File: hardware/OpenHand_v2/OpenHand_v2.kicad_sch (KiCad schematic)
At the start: 56 parts, among them J1 CONN_MOTOR_1, J10 CONN_FDBK_2, J11 CONN_EMG_2, J12 CONN_POS_3, J13 CONN_JTAG, J2 CONN_MOTOR_2, J3 CONN_BATT, J4 CONN_POS_1, J5 USB_C_CONN, J6 CONN_MOTOR_3, J7 CONN_FDBK_1, J8 CONN_EMG_1, J9 CONN_POS_2, SW1 BTN_RST, SW3 SW_Push, U1 STM32F103RETx, Y1 16MHz

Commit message: Update V2 schematic and start PCB layout
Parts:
- removed J5: USB_C_CONN, Connector_USB:USB_C_Receptacle_G-Switch_GT-USB-7010ASV, symbol Connector:USB_C_Receptacle_USB2.0
- removed JP2: JMPR_LED_1, Jumper:SolderJumper-2_P1.3mm_Bridged_RoundedPad1.0x1.5mm, symbol Jumper:SolderJumper_2_Bridged
- removed JP3: JMPR_BTN_1, Jumper:SolderJumper-2_P1.3mm_Bridged_RoundedPad1.0x1.5mm, symbol Jumper:SolderJumper_2_Bridged
- removed JP4: JMPR_LED_2, Jumper:SolderJumper-2_P1.3mm_Bridged_RoundedPad1.0x1.5mm, symbol Jumper:SolderJumper_2_Bridged
- removed R4: 1.5k, Resistor_SMD:R_0805_2012Metric, symbol Device:R
- removed TP12: TP_UC_PIN_PA5, TestPoint:TestPoint_Pad_D1.0mm, symbol Connector:TestPoint_Small
- removed TP13: TP_UC_PIN_PD2, TestPoint:TestPoint_Pad_D1.0mm, symbol Connector:TestPoint_Small
- removed TP14: TP_UC_PIN_PA6, TestPoint:TestPoint_Pad_D1.0mm, symbol Connector:TestPoint_Small
- removed TP20: TP_UC_PIN_PC12, TestPoint:TestPoint_Pad_D1.0mm, symbol Connector:TestPoint_Small
- removed TP23: TP_UC_PIN_PB12, TestPoint:TestPoint_Pad_D1.0mm, symbol Connector:TestPoint_Small
- added J5: CONN_USB_C, Connector_USB:USB_C_Receptacle_G-Switch_GT-USB-7010ASV, symbol Connector:USB_C_Receptacle_USB2.0_16P
- added R3: 1.5k, Resistor_SMD:R_0805_2012Metric, symbol Device:R
- J10: renamed from J13; footprint (none) -> Connector_PinHeader_2.54mm:PinHeader_1x06_P2.54mm_Vertical
- J12: renamed from J11; footprint Connector_JST:JST_EH_S3B-EH_1x03_P2.50mm_Horizontal -> Connector_PinHeader_2.54mm:PinHeader_1x03_P2.54mm_Vertical
- J13: renamed from J12; footprint Connector_JST:JST_EH_S3B-EH_1x03_P2.50mm_Horizontal -> Connector_PinHeader_2.54mm:PinHeader_1x03_P2.54mm_Vertical
- J4, J8, J9: footprint Connector_JST:JST_EH_S3B-EH_1x03_P2.50mm_Horizontal -> Connector_PinHeader_2.54mm:PinHeader_1x03_P2.54mm_Vertical
- Y1: footprint (none) -> Crystal:Crystal_SMD_3225-4Pin_3.2x2.5mm; Footprint Desc (none) -> SMD3225-4P
- renumbered C3 to C2, C4 to C3, C5 to C4, C6 to C5, C40 to C6, C2 to C7, C15 to C8, J10 to J11, R2 to R1, R11 to R10, R12 to R11, R3 to R2, R6 to R4, R7 to R5, R8 to R6, R9 to R7, R10 to R8, R5 to R9, SW3 to SW2, TP18 to TP1, TP19 to TP2, TP21 to TP3, TP22 to TP4
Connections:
- net Earth is gone; now on net GND: C1.2, C2.2, C3.2, C4.2, C5.2, C6.2, H1.1, H2.1, H3.1, H4.1, J10.1 (Pin_1), J12.1 (Pin_1), J13.1 (Pin_1), J3.1 (Pin_1), J4.1 (Pin_1), J8.1 (Pin_1), J9.1 (Pin_1), R1.2, R11.1, R2.2, R7.2, R8.2, R9.1, RV1.1, RV2.1, SW1.2, SW2.2, U1.12 (VSSA), U1.18 (VSS), U1.31 (VSS), U1.47 (VSS), U1.63 (VSS)
- net HW_REV_04 is gone; now on net HSE_IN: U1.5 (PD0)
- net +3V3: now also R3.2
- net +5V: now also J5.A4 (VBUS), J5.A9 (VBUS), J5.B4 (VBUS), J5.B9 (VBUS)
- net BTN_01: now also R6.2, SW2.1
- net LED_1: now also D1.2 (A)
- net LED_2: now also D2.2 (A)
- net USB_D+: now also J5.A6 (D+), J5.B6 (D+), R3.1
- net USB_D-: now also J5.A7 (D-), J5.B7 (D-)
- net HSE_IN: now reaches Y1.1
- net HSE_IN: now also C7.1
- net GND: now reaches Y1.2
- net GND: now also C7.2, C8.2, Y1.4, J5.A1 (GND), J5.A12 (GND), J5.B1 (GND), J5.B12 (GND)
- net HSE_OUT: now reaches Y1.3
- net HSE_OUT: now also C8.1, U1.6 (PD1)
- net LED_1_K: now reaches D1.1 (K), R7.1
- net USB_CC2: now reaches R2.1
- net USB_CC2: now also J5.B5 (CC2)
- net USB_CC1: now reaches R1.1
- net USB_CC1: now also J5.A5 (CC1)
- net UC_BOOT: now reaches R9.2, U1.60 (BOOT0)
- net LED_2_K: now reaches D2.1 (K), R8.1
- net HW_REV_01: no longer names the net of U1.2 (PC13)
- net HW_REV_02: no longer names the net of U1.3 (PC14)
- net HW_REV_03: no longer names the net of U1.4 (PC15)
- net TRIM_POT_03: no longer names the net of U1.14 (PA0)
- no-connect marks 4 -> 12
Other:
- note added: "HSE - External oscillator CL = 2*(CL0-Cs) = 2*(10-5)pF = 10pF"
- note added: "TODO: - Add JLC order number on PCB - Double-check all the footprint sizes and dimensions - Order additional parts (osc, caps, buttons...)"
- note removed: "TODO: - Add JLC order number on PCB - Double-check all the footprint sizes and dimensions"
- note removed: "TODO: clock oscillator"
- moved on the sheet: C7, C8, D1, D2, R1, R10, R11, R2, R6, R7, R8, R9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

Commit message: Add V2 PCB and update CubeIDE config for V2
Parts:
- removed J10: CONN_JTAG, Connector_PinHeader_2.54mm:PinHeader_1x06_P2.54mm_Vertical, symbol Connector_Generic:Conn_01x06
- added C6: 100n, Capacitor_SMD:C_0805_2012Metric, symbol Device:C
- added J12: CONN_SWD, Connector_PinHeader_2.54mm:PinHeader_1x04_P2.54mm_Vertical, symbol Connector_Generic:Conn_01x04
- added TP1: TP_UC_PA6, TestPoint:TestPoint_Pad_D1.0mm, symbol Connector:TestPoint_Small
- added TP10: TP_GND_5, TestPoint:TestPoint_Pad_1.5x1.5mm, symbol Connector:TestPoint_Small
- added TP11: TP_GND_6, TestPoint:TestPoint_Pad_1.5x1.5mm, symbol Connector:TestPoint_Small
- added TP14: TP_UC_PB12, TestPoint:TestPoint_Pad_D1.0mm, symbol Connector:TestPoint_Small
- added TP4: TP_UC_PC13, TestPoint:TestPoint_Pad_D1.0mm, symbol Connector:TestPoint_Small
- added TP5: TP_UC_PC15, TestPoint:TestPoint_Pad_D1.0mm, symbol Connector:TestPoint_Small
- added TP6: TP_GND_1, TestPoint:TestPoint_Pad_1.5x1.5mm, symbol Connector:TestPoint_Small
- added TP7: TP_GND_2, TestPoint:TestPoint_Pad_1.5x1.5mm, symbol Connector:TestPoint_Small
- added TP8: TP_GND_3, TestPoint:TestPoint_Pad_1.5x1.5mm, symbol Connector:TestPoint_Small
- added TP9: TP_GND_4, TestPoint:TestPoint_Pad_1.5x1.5mm, symbol Connector:TestPoint_Small
- TP12: renamed from TP3; footprint TestPoint:TestPoint_Pad_D1.0mm -> TestPoint:TestPoint_Pad_D2.0mm
- TP13: renamed from TP4; footprint TestPoint:TestPoint_Pad_D1.0mm -> TestPoint:TestPoint_Pad_D2.0mm
- TP2: renamed from TP1; footprint TestPoint:TestPoint_Pad_D1.0mm -> TestPoint:TestPoint_Pad_D2.0mm
- TP3: renamed from TP2; footprint TestPoint:TestPoint_Pad_D1.0mm -> TestPoint:TestPoint_Pad_D2.0mm
- renumbered C6 to C7, C7 to C8, C8 to C9, J11 to J10, J12 to J11
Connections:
- net +3V3: now also C6.1, J12.4 (Pin_4)
- net GND: now also C6.2, J12.1 (Pin_1), TP10.1, TP11.1, TP6.1, TP7.1, TP8.1, TP9.1
- net HAPTIC_01_DIR: now also U1.34 (PB13); no longer U1.36 (PB15)
- net HAPTIC_01_PWM: now also U1.35 (PB14); no longer U1.37 (PC6)
- net HAPTIC_02_DIR: now also U1.36 (PB15); no longer U1.34 (PB13)
- net HAPTIC_02_PWM: now also U1.37 (PC6); no longer U1.35 (PB14)
- net HAPTIC_EN: now also U1.23 (PA7); no longer U1.26 (PB0)
- net MOTOR_01_DIR: now also U1.38 (PC7); no longer U1.42 (PA9)
- net MOTOR_01_EN: now also U1.25 (PC5); no longer U1.23 (PA7)
- net MOTOR_01_FAULT: now also U1.28 (PB2); no longer U1.27 (PB1)
- net MOTOR_01_PWM: now also U1.39 (PC8); no longer U1.43 (PA10)
- net MOTOR_02_EN: now also U1.27 (PB1); no longer U1.24 (PC4)
- net MOTOR_02_FAULT: now also U1.26 (PB0); no longer U1.28 (PB2)
- net MOTOR_03_DIR: now also U1.42 (PA9); no longer U1.38 (PC7)
- net MOTOR_03_EN: now also U1.29 (PB10); no longer U1.25 (PC5)
- net MOTOR_03_FAULT: now also U1.24 (PC4); no longer U1.29 (PB10)
- net MOTOR_03_PWM: now also U1.43 (PA10); no longer U1.39 (PC8)
- net at U1.2 (PC13): now also TP4.1
- net at U1.22 (PA6): now also TP1.1
- net at U1.33 (PB12): now also TP14.1
- net at U1.4 (PC15): now also TP5.1
- net JTAG_RST: no longer names the net of U1.56 (PB4)
- net JTAG_TCK renamed SWCLK
- net SWCLK: now also J12.3 (Pin_3)
- net JTAG_TDI: no longer names the net of U1.50 (PA15)
- net JTAG_TDO: no longer names the net of U1.55 (PB3)
- net JTAG_TMS renamed SWDIO
- net SWDIO: now also J12.2 (Pin_2)
- no-connect marks 12 -> 11
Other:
- note added: "Can be useful sometimes. To be placed around the board"
- note added: "GROUND TEST POINTS"
- note added: "Serial Wire Debug"
- note added: "Serial Wire Debug (SWD)"
- note removed: "JTAG"
- note removed: "JTAG debugging"
- moved on the sheet: C7

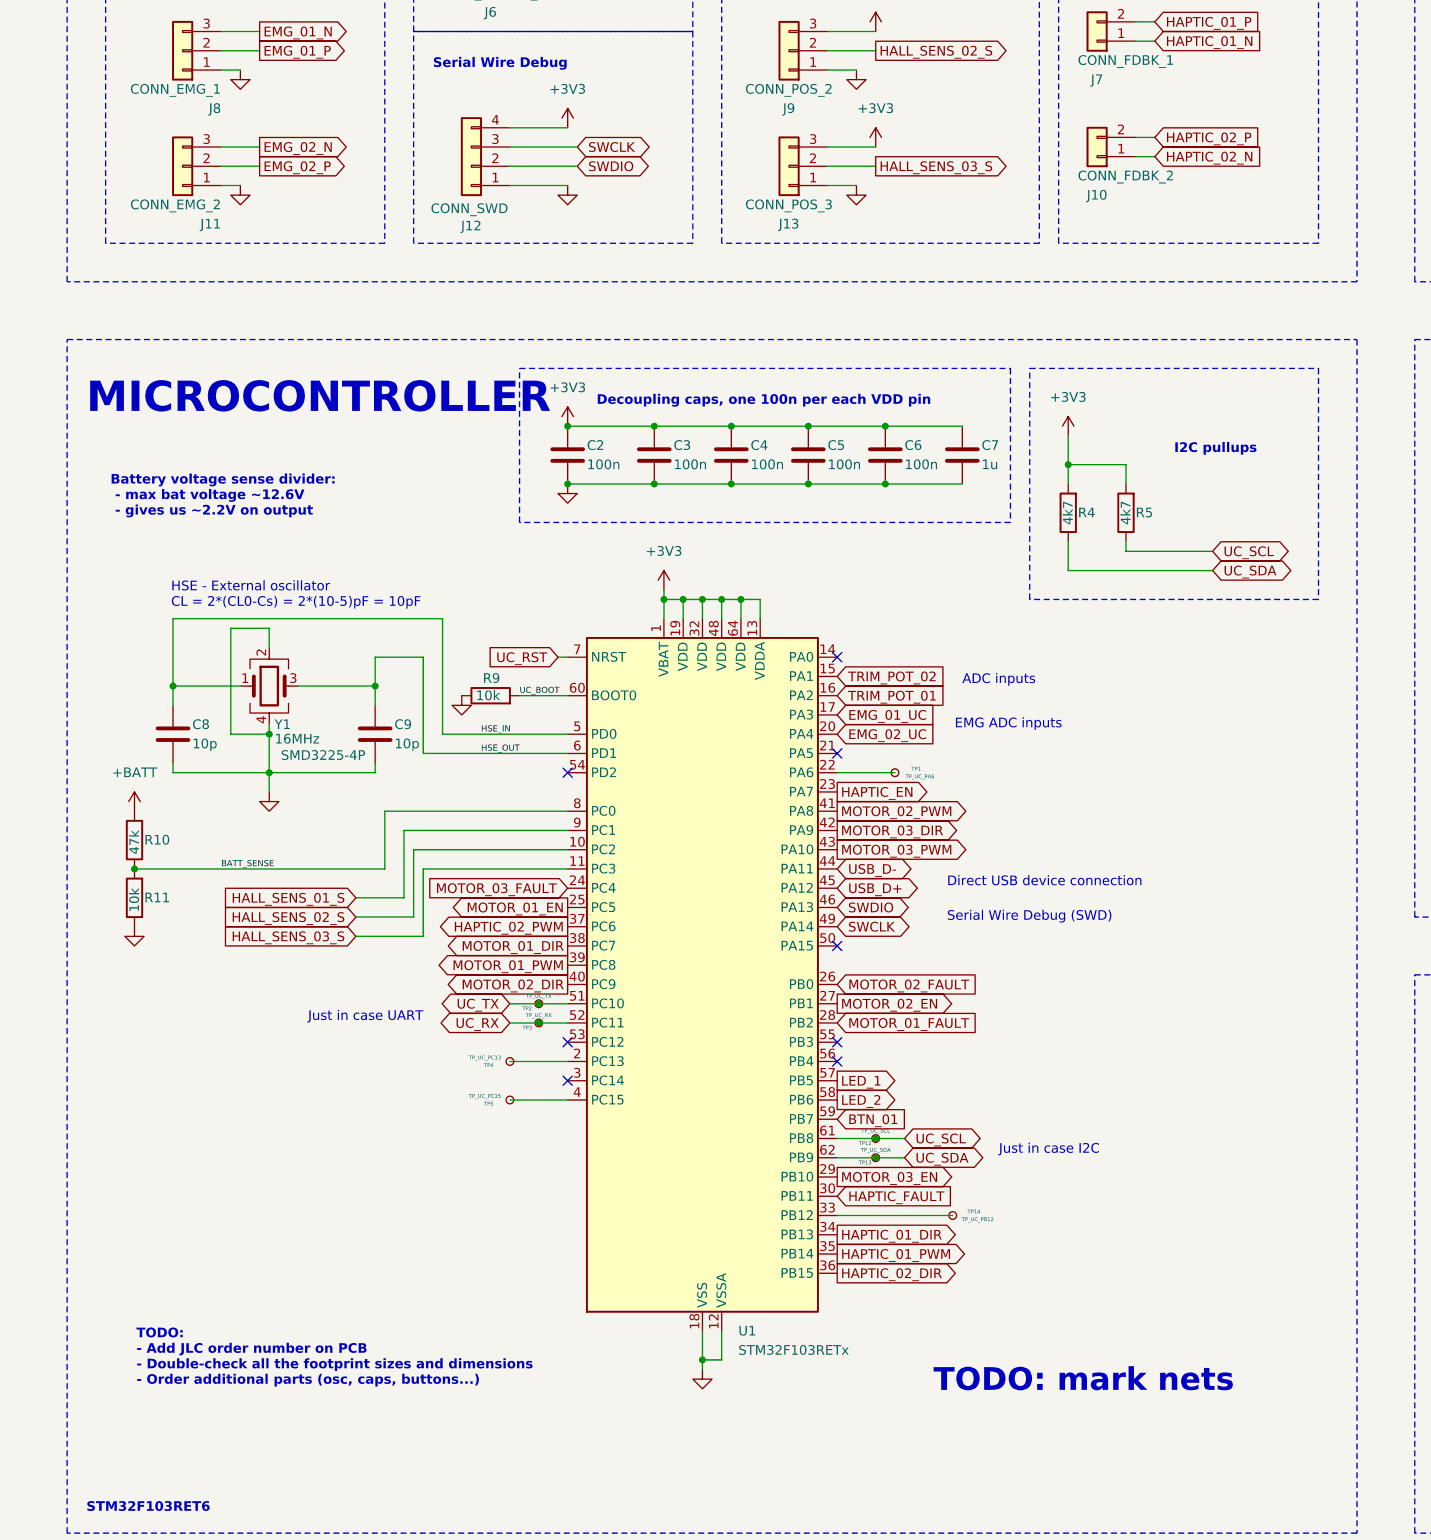
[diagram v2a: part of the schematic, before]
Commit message: Update PCB and order from JLCPCB
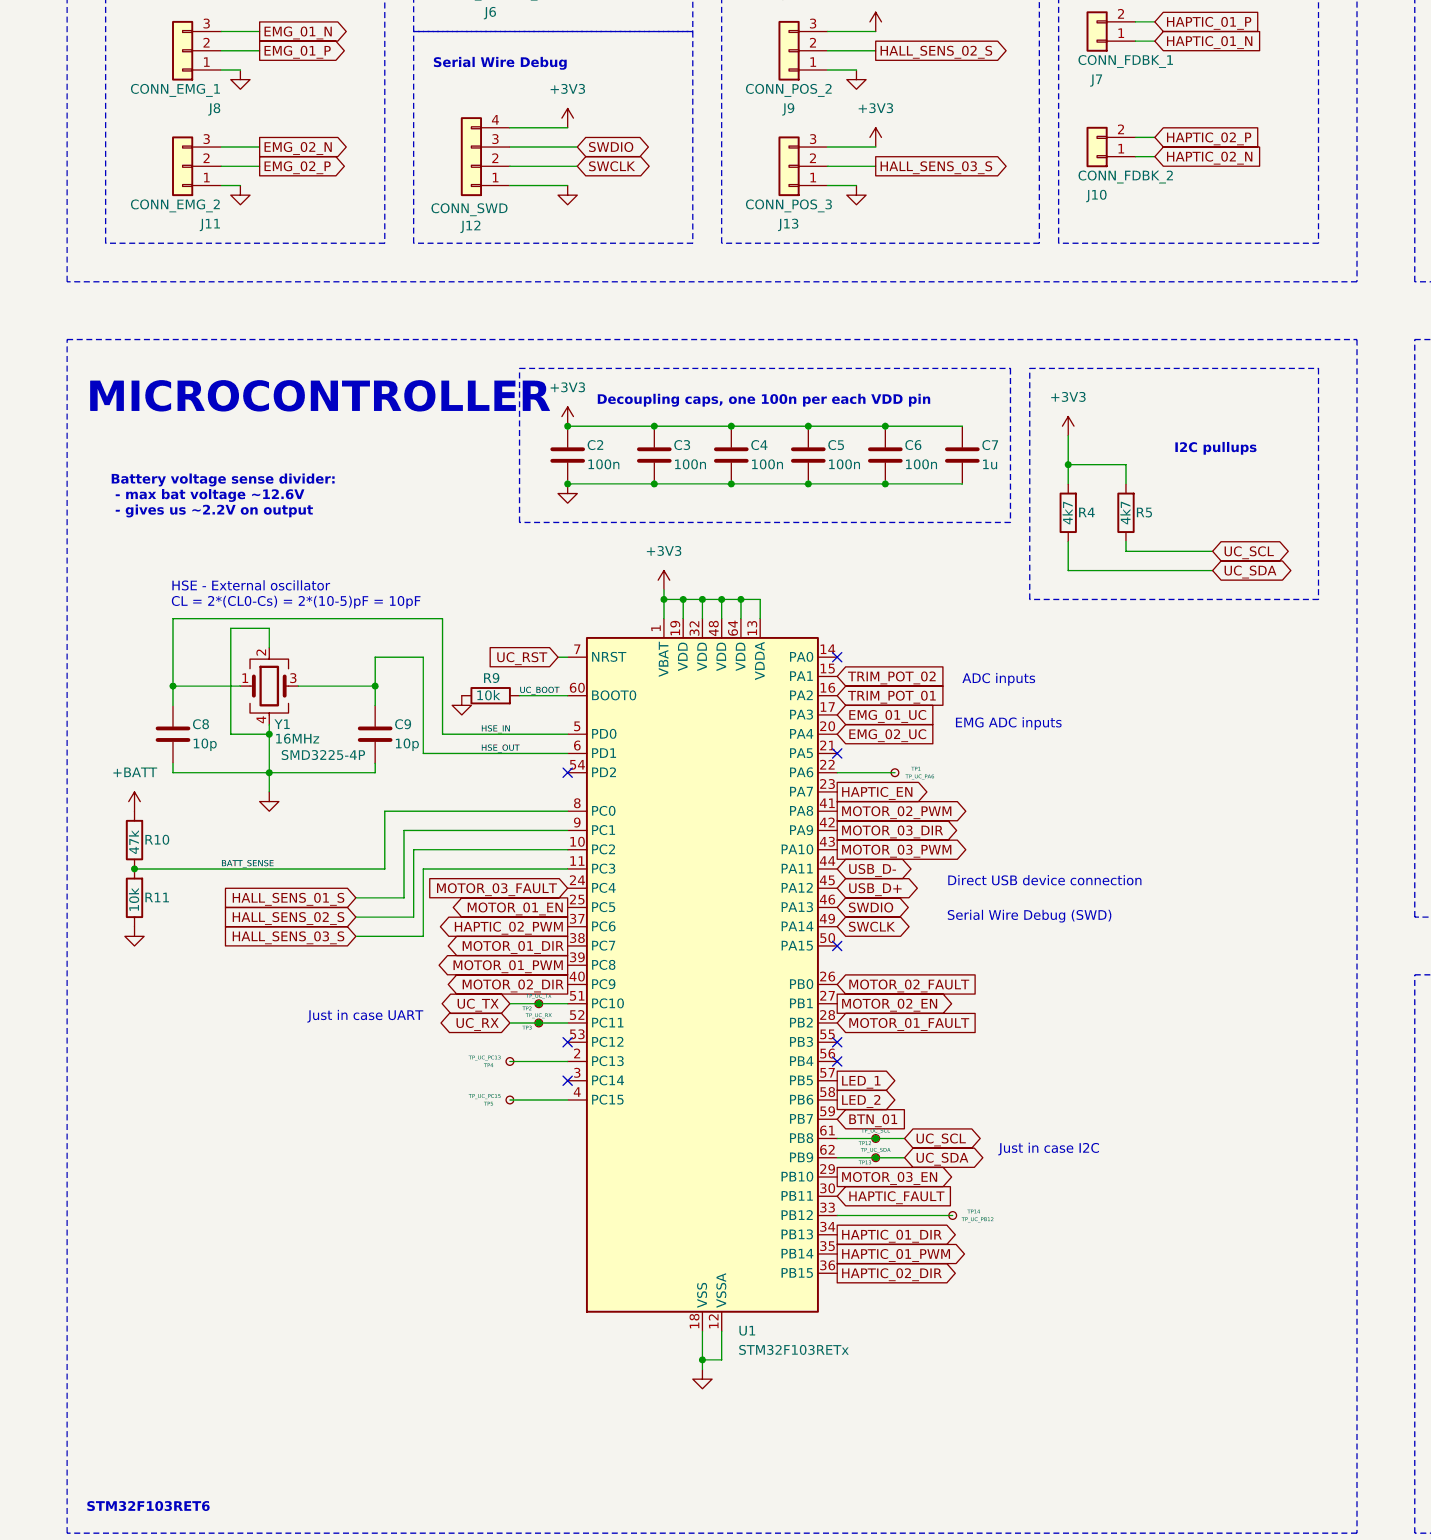
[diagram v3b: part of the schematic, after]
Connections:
- net SWCLK: now also J12.2 (Pin_2); no longer J12.3 (Pin_3)
- net SWDIO: now also J12.3 (Pin_3); no longer J12.2 (Pin_2)
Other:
- note removed: "TODO: - Add JLC order number on PCB - Double-check all the footprint sizes and dimensions - Order additional parts (osc, caps, buttons...)"
- note removed: "TODO: mark nets"
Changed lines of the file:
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@@
-		)
-	)
-	(text "TODO: mark nets"
-		(exclude_from_sim no)
-		(at 134.62 256.032 0)
-		(effects
-			(font
-				(size 3 3)
-				(thickness 0.6)
-				(bold yes)
-			)
-			(justify left bottom)
 		)
 	)
@@
 		(exclude_from_sim no)
 		(at 200.66 271.78 0)
-		(effects
-			(font
-				(size 1.27 1.27)
-				(bold yes)
-			)
-			(justify left bottom)
-		)
-	)
-	(text "TODO:\n- Add JLC order number on PCB\n- Double-check all the footprint sizes and dimensions\n- Order additional parts (osc, caps, buttons...)"
-		(exclude_from_sim no)
-		(at 29.464 255.016 0)
 		(effects
 			(font
@@
 		)
 	)
-	(global_label "EMG_01_UC"
-		(shape input)
-		(at 121.92 166.37 0)
-		(fields_autoplaced yes)
-		(effects
-			(font
-				(size 1.27 1.27)
-			)
-			(justify left)
-		)
-		(property "Intersheetrefs" "${INTERSHEET_REFS}"
-			(at 135.7303 166.37 0)
-			(effects
-				(font
-					(size 1.27 1.27)
-				)
-				(justify left)
-				(hide yes)
-			)
-		)
-	)
-	(global_label "SWDIO"
+	(global_label "SWCLK"
 		(shape bidirectional)
 		(at 87.63 93.98 0)
@@
 		)
 		(property "Intersheetrefs" "${INTERSHEET_REFS}"
-			(at 97.5927 93.98 0)
+			(at 97.9555 93.98 0)
+			(effects
+				(font
+					(size 1.27 1.27)
+				)
+				(justify left)
+				(hide yes)
+			)
+		)
+	)
+	(global_label "EMG_01_UC"
+		(shape input)
+		(at 121.92 166.37 0)
+		(fields_autoplaced yes)
+		(effects
+			(font
+				(size 1.27 1.27)
+			)
+			(justify left)
+		)
+		(property "Intersheetrefs" "${INTERSHEET_REFS}"
+			(at 135.7303 166.37 0)
 			(effects
 				(font
@@
 		)
 	)
-	(global_label "SWCLK"
-		(shape bidirectional)
-		(at 87.63 91.44 0)
-		(fields_autoplaced yes)
-		(effects
-			(font
-				(size 1.27 1.27)
-			)
-			(justify left)
-		)
-		(property "Intersheetrefs" "${INTERSHEET_REFS}"
-			(at 97.9555 91.44 0)
-			(effects
-				(font
-					(size 1.27 1.27)
-				)
-				(justify left)
-				(hide yes)
-			)
-		)
-	)
 	(global_label "UC_SCL"
 		(shape bidirectional)
@@
 			(effects
 				(font
+					(size 1.27 1.27)
+				)
+				(justify left)
+				(hide yes)
+			)
+		)
+	)
+	(global_label "SWDIO"
+		(shape bidirectional)
+		(at 87.63 91.44 0)
+		(fields_autoplaced yes)
+		(effects
+			(font
+				(size 1.27 1.27)
+			)
+			(justify left)
+		)
+		(property "Intersheetrefs" "${INTERSHEET_REFS}"
+			(at 97.5927 91.44 0)
+			(effects
+				(font
